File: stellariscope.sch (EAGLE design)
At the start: 37 parts, among them U1 74238, U10 74AHC1G126DBV, U2 74238, U3 TLC5947PWP, U4 TLC59213, U5 741G79DCT, U6 74AHC1G126DBV, U7 74AHC1G126DBV, U8 74AHC1G32DBV, U9 74AHC1G32DBV

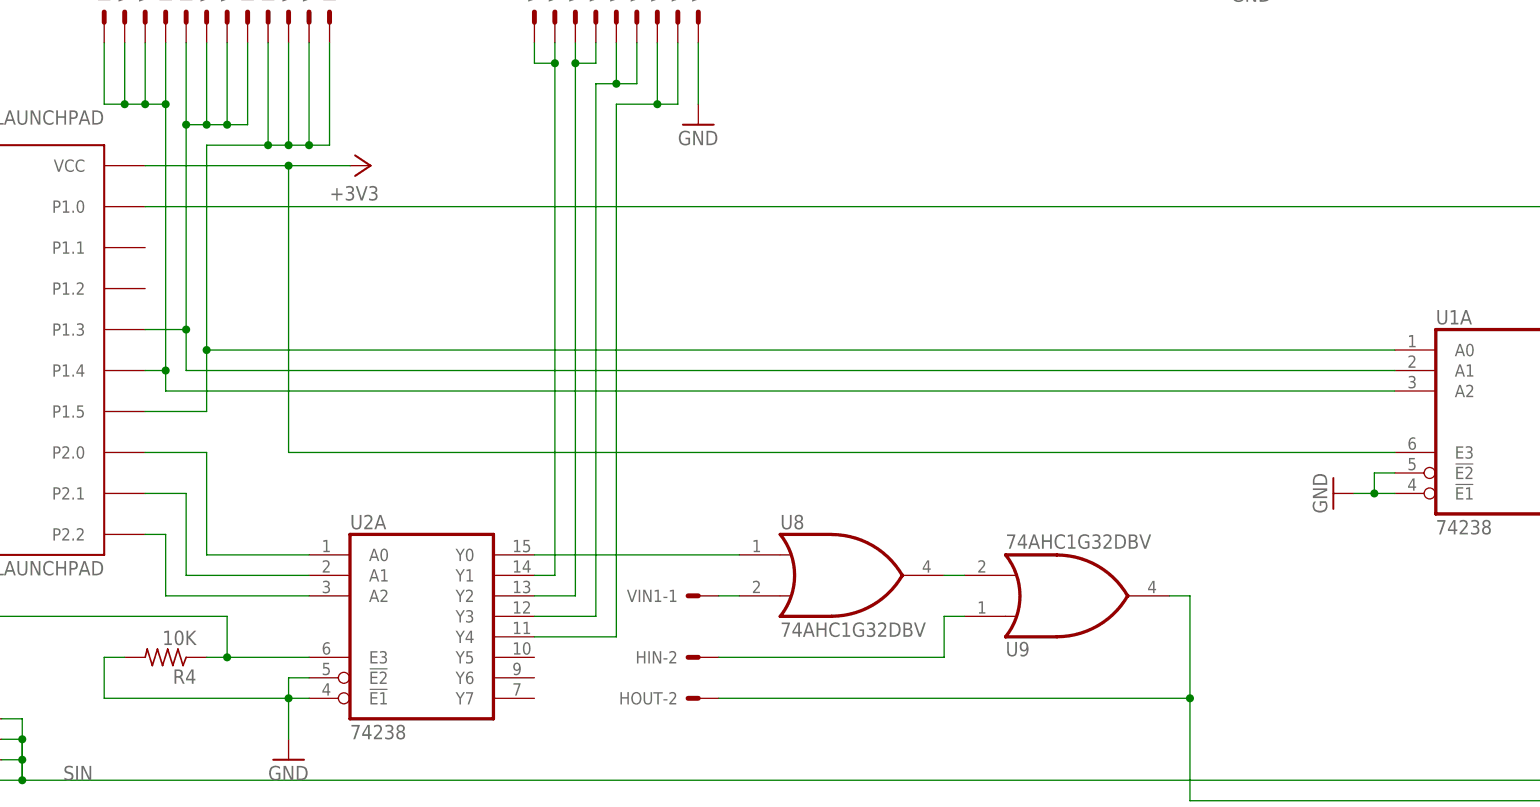
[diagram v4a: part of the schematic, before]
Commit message: Fixed the serial issue right this time, miscellaneous test code changes (not done)
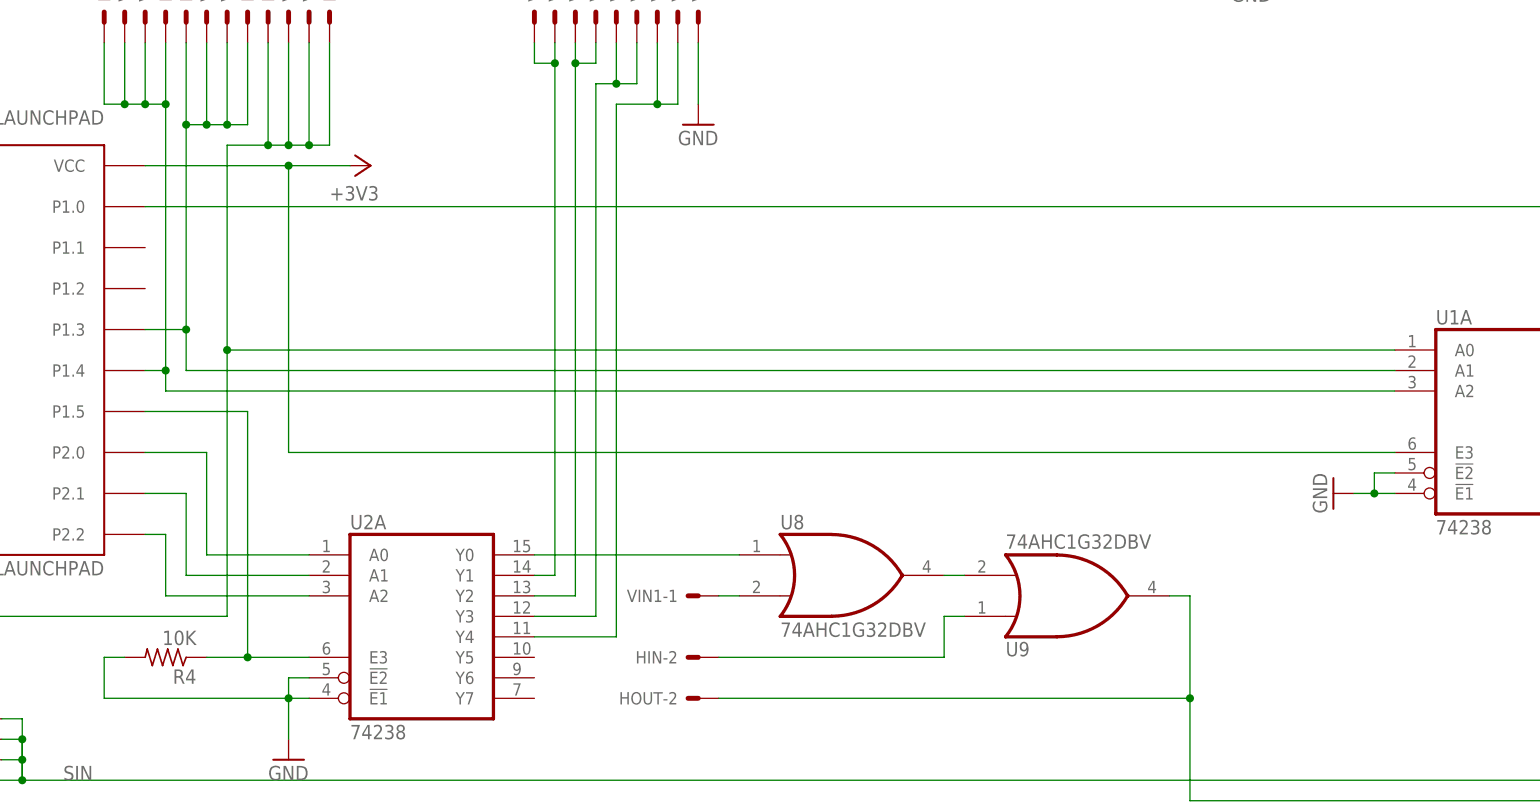
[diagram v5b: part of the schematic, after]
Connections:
- net N$29: now also LAUNCHPAD.P1.5; no longer LAUNCHPAD.P2.3
- net N$36: now also LAUNCHPAD.P2.3; no longer LAUNCHPAD.P1.5
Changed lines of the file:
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@@
 <segment>
 <pinref part="U2" gate="A" pin="E3"/>
-<wire x1="134.62" y1="137.16" x2="137.16" y2="137.16" width="0.1524" layer="91"/>
+<wire x1="134.62" y1="137.16" x2="139.7" y2="137.16" width="0.1524" layer="91"/>
 <pinref part="R4" gate="G$1" pin="1"/>
-<pinref part="LAUNCHPAD" gate="G$1" pin="P2.3"/>
-<wire x1="137.16" y1="137.16" x2="147.32" y2="137.16" width="0.1524" layer="91"/>
-<wire x1="91.44" y1="152.4" x2="88.9" y2="152.4" width="0.1524" layer="91"/>
-<wire x1="88.9" y1="152.4" x2="88.9" y2="142.24" width="0.1524" layer="91"/>
-<wire x1="88.9" y1="142.24" x2="137.16" y2="142.24" width="0.1524" layer="91"/>
-<wire x1="137.16" y1="142.24" x2="137.16" y2="137.16" width="0.1524" layer="91"/>
-<junction x="137.16" y="137.16"/>
+<wire x1="139.7" y1="137.16" x2="147.32" y2="137.16" width="0.1524" layer="91"/>
+<wire x1="139.7" y1="167.64" x2="139.7" y2="137.16" width="0.1524" layer="91"/>
+<junction x="139.7" y="137.16"/>
+<pinref part="LAUNCHPAD" gate="G$1" pin="P1.5"/>
+<wire x1="139.7" y1="167.64" x2="127" y2="167.64" width="0.1524" layer="91"/>
 </segment>
 </net>
@@
 <segment>
 <pinref part="U1" gate="A" pin="A0"/>
-<wire x1="134.62" y1="175.26" x2="281.94" y2="175.26" width="0.1524" layer="91"/>
-<wire x1="134.62" y1="175.26" x2="134.62" y2="200.66" width="0.1524" layer="91"/>
+<wire x1="137.16" y1="175.26" x2="281.94" y2="175.26" width="0.1524" layer="91"/>
+<wire x1="137.16" y1="175.26" x2="137.16" y2="200.66" width="0.1524" layer="91"/>
 <pinref part="HOUT" gate="-7" pin="S"/>
-<wire x1="134.62" y1="200.66" x2="142.24" y2="200.66" width="0.1524" layer="91"/>
+<wire x1="137.16" y1="200.66" x2="142.24" y2="200.66" width="0.1524" layer="91"/>
 <wire x1="142.24" y1="200.66" x2="142.24" y2="213.36" width="0.1524" layer="91"/>
 <pinref part="HIN" gate="-7" pin="S"/>
@@
 <junction x="144.78" y="200.66"/>
 <junction x="147.32" y="200.66"/>
-<pinref part="LAUNCHPAD" gate="G$1" pin="P1.5"/>
-<wire x1="127" y1="167.64" x2="134.62" y2="167.64" width="0.1524" layer="91"/>
-<wire x1="134.62" y1="167.64" x2="134.62" y2="175.26" width="0.1524" layer="91"/>
-<junction x="134.62" y="175.26"/>
+<wire x1="137.16" y1="142.24" x2="137.16" y2="175.26" width="0.1524" layer="91"/>
+<junction x="137.16" y="175.26"/>
+<pinref part="LAUNCHPAD" gate="G$1" pin="P2.3"/>
+<wire x1="91.44" y1="152.4" x2="88.9" y2="152.4" width="0.1524" layer="91"/>
+<wire x1="88.9" y1="152.4" x2="88.9" y2="142.24" width="0.1524" layer="91"/>
+<wire x1="88.9" y1="142.24" x2="137.16" y2="142.24" width="0.1524" layer="91"/>
 </segment>
 </net>

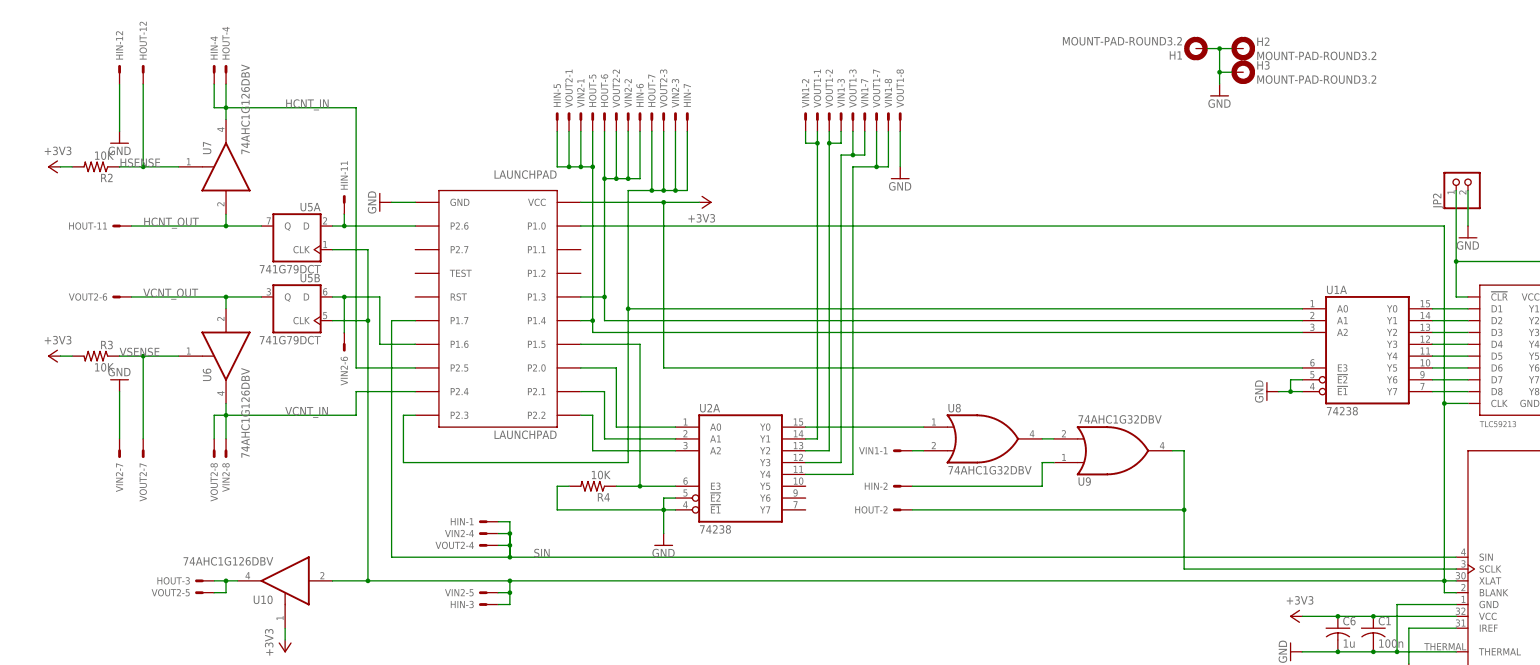
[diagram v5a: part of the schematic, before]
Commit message: -- added pull-downs to all inputs from the Launchpad -- added delay filters to counting lines so they work now.
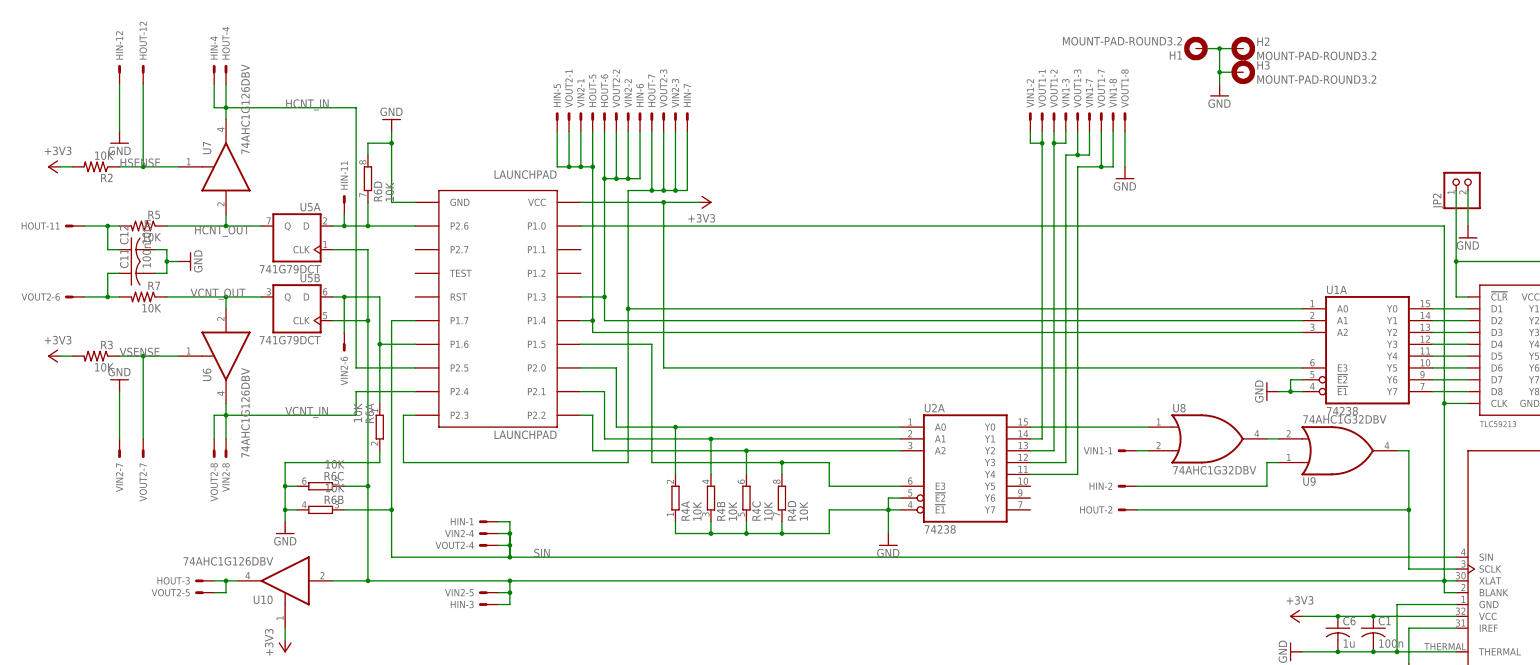
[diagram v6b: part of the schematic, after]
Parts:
- added C11, C12: 100n, resistor:C-USC0603
- added R5, R7: 10K, resistor:R-US_R0603
- added R6: 10K, res-cap-arrays:4R-NCTS742C083
- C10: PARTNO (none) -> C3216Y5V1A106Z/0.85
- C9: PARTNO (none) -> C3216X5R1E106M
- H1, H2, H3: BOM (none) -> EXCLUDE
- JP1: DNP (none) -> T
- R4: device resistor:R-US_R0603 -> res-cap-arrays:4R-NCTS742C083; PARTNO RMCF0603FT10K0 -> 742C083103JPTR
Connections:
- new net N$28: C12.1, HOUT-11.S, R5.2
- new net N$42: C11.1, R7.2, VOUT2-6.S
- net GND: now also C11.2, C12.2, R4A.1, R4B.1, R4C.1, R4D.1, R6A.2, R6B.2, R6C.2, R6D.2; no longer R4.2
- net HCNT_OUT: now also R5.1; no longer HOUT-11.S
- net N$29: now also R4D.2; no longer R4.1
- net N$31: now also R4A.2
- net N$32: now also R4B.2
- net N$33: now also R4C.2
- net N$37: now also R6D.1
- net N$38: now also R6A.1
- net SIN: now also R6B.1
- net VCNT_OUT: now also R7.1; no longer VOUT2-6.S
- net XLAT: now also R6C.1
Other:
- moved on the sheet: HIN-2, HOUT-11, HOUT-2, U2A, U8, U9, VIN1-1, VIN1-2, VIN1-3, VIN1-7, VIN1-8, VOUT1-1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

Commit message: Committing everything to date...
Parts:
- C10: PARTNO C3216Y5V1A106Z/0.85 -> C3216X5R1E106M
- JP1, JP2: PARTNO (none) -> *
- U1, U2: PARTNO SN74AHC138PWR -> CD74HC238PWR
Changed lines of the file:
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@@
 </part>
 <part name="U1" library="ti-stuff" deviceset="74*238" device="">
-<attribute name="PARTNO" value="SN74AHC138PWR"/>
+<attribute name="PARTNO" value="CD74HC238PWR"/>
 </part>
 <part name="U2" library="ti-stuff" deviceset="74*238" device="">
-<attribute name="PARTNO" value="SN74AHC138PWR"/>
+<attribute name="PARTNO" value="CD74HC238PWR"/>
 </part>
 <part name="U3" library="logos-led-drivers" deviceset="TLC5947" device="PWP">
@@
 <part name="JP1" library="pinhead" deviceset="PINHD-1X3" device="">
 <attribute name="DNP" value="T"/>
+<attribute name="PARTNO" value="*"/>
 </part>
 <part name="P+2" library="supply1" deviceset="+5V" device=""/>
 <part name="GND19" library="supply1" deviceset="GND" device=""/>
-<part name="JP2" library="pinhead-1" deviceset="PINHD-1X2" device="_2.54-90°"/>
+<part name="JP2" library="pinhead-1" deviceset="PINHD-1X2" device="_2.54-90°">
+<attribute name="PARTNO" value="*"/>
+</part>
 <part name="C9" library="resistor" deviceset="C-US" device="C1210" value="10u">
 <attribute name="PARTNO" value="C3216X5R1E106M"/>
 </part>
 <part name="C10" library="resistor" deviceset="C-US" device="C1210" value="10u">
-<attribute name="PARTNO" value="C3216Y5V1A106Z/0.85"/>
+<attribute name="PARTNO" value="C3216X5R1E106M"/>
 </part>
 <part name="GND20" library="supply1" deviceset="GND" device=""/>
@@
 <instance part="JP1" gate="A" x="233.68" y="48.26" rot="R180">
 <attribute name="DNP" x="233.68" y="48.26" size="1.778" layer="96" rot="R180" display="off"/>
+<attribute name="PARTNO" x="233.68" y="48.26" size="1.778" layer="96" display="off"/>
 </instance>
 <instance part="P+2" gate="1" x="246.38" y="50.8" rot="R270"/>
 <instance part="GND19" gate="1" x="243.84" y="40.64"/>
-<instance part="JP2" gate="G$1" x="317.5" y="203.2" rot="R90"/>
+<instance part="JP2" gate="G$1" x="317.5" y="203.2" rot="R90">
+<attribute name="PARTNO" x="317.5" y="203.2" size="1.778" layer="96" display="off"/>
+</instance>
 <instance part="C9" gate="G$1" x="355.6" y="187.96">
 <attribute name="PARTNO" x="355.6" y="187.96" size="1.778" layer="96" display="off"/>
